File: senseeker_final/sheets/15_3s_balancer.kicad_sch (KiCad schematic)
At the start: 32 parts, among them J1 Conn_01x02, J6 Conn_01x04, Q1 AO4892, Q2 BSS84, SW1 TS-1088R-02026, U1 NTC10K/0805/F, U4 BQ76920PW

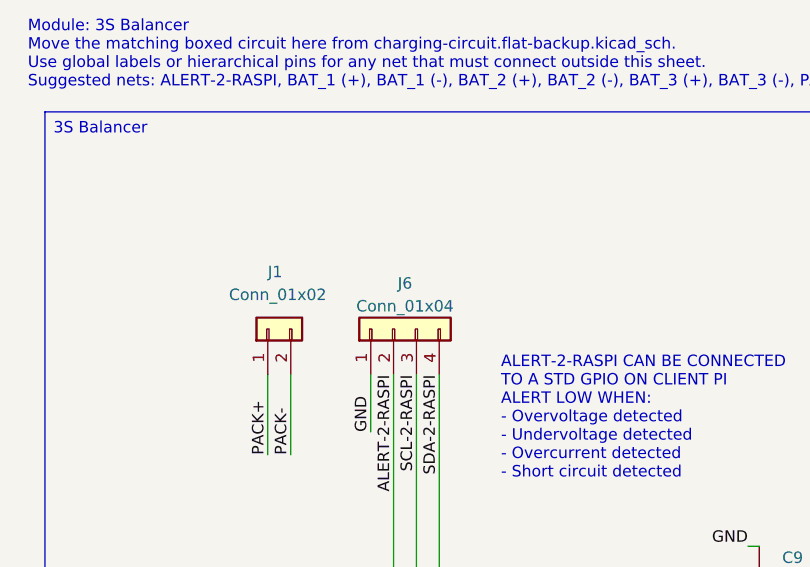
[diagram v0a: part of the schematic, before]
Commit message: fixed annotations
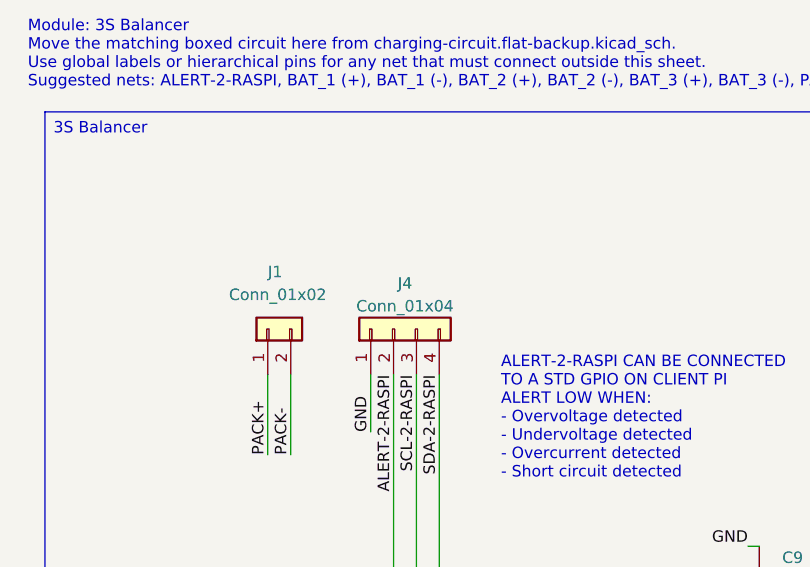
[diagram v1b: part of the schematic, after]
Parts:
- renumbered J6 to J4
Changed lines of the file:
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@@
 		(dnp no)
 		(fields_autoplaced yes)
-		(property "Reference" "J6"
+		(property "Reference" "J4"
 			(at 67.31 50.8 90)
 			(show_name no)
@@
 			(project "senseeker_final"
 				(path "/529bc8a5-ffae-43ac-972d-caccc3afab85/cff05046-5666-496e-bdc0-c674fdf4f5c2"
-					(reference "J6")
+					(reference "J4")
 					(unit 1)
 				)

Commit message: finished for tn
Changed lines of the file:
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@@
 	(text "THIS PART OF THE CIRCUIT IS PROTECTION AGAINST OVER/UNDER VOLTAGE/CURRENT."
 		(exclude_from_sim no)
-		(at 69.596 167.386 0)
+		(at 69.85 179.324 0)
 		(effects
 			(font
@@
 		)
 	)
-	(text_box "3S Balancer\n"
-		(exclude_from_sim no)
-		(at 27.305 31.75 0)
-		(size 228.6 149.86)
-		(margins 0.9525 0.9525 0.9525 0.9525)
-		(stroke
-			(width 0)
-			(type solid)
-		)
-		(fill
-			(type none)
-		)
-		(effects
-			(font
-				(size 1.27 1.27)
-			)
-			(justify left top)
-		)
-	)
